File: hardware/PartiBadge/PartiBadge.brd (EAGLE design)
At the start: 101.6 x 101.6 mm, 23 parts, among them J1 I2C, J2 Supply

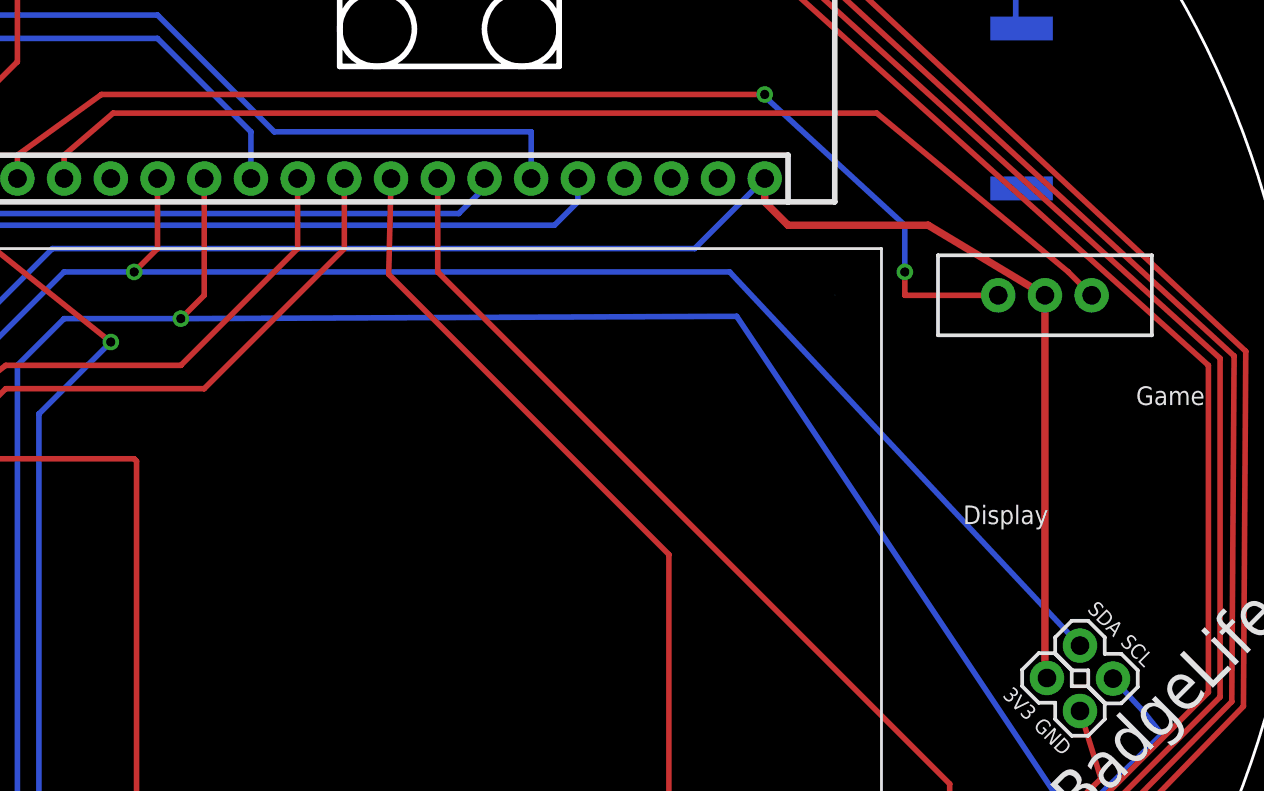
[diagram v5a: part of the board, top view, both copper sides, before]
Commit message: Add clr to 3v3 line next to switch; closes #9; add text to back; closes #8
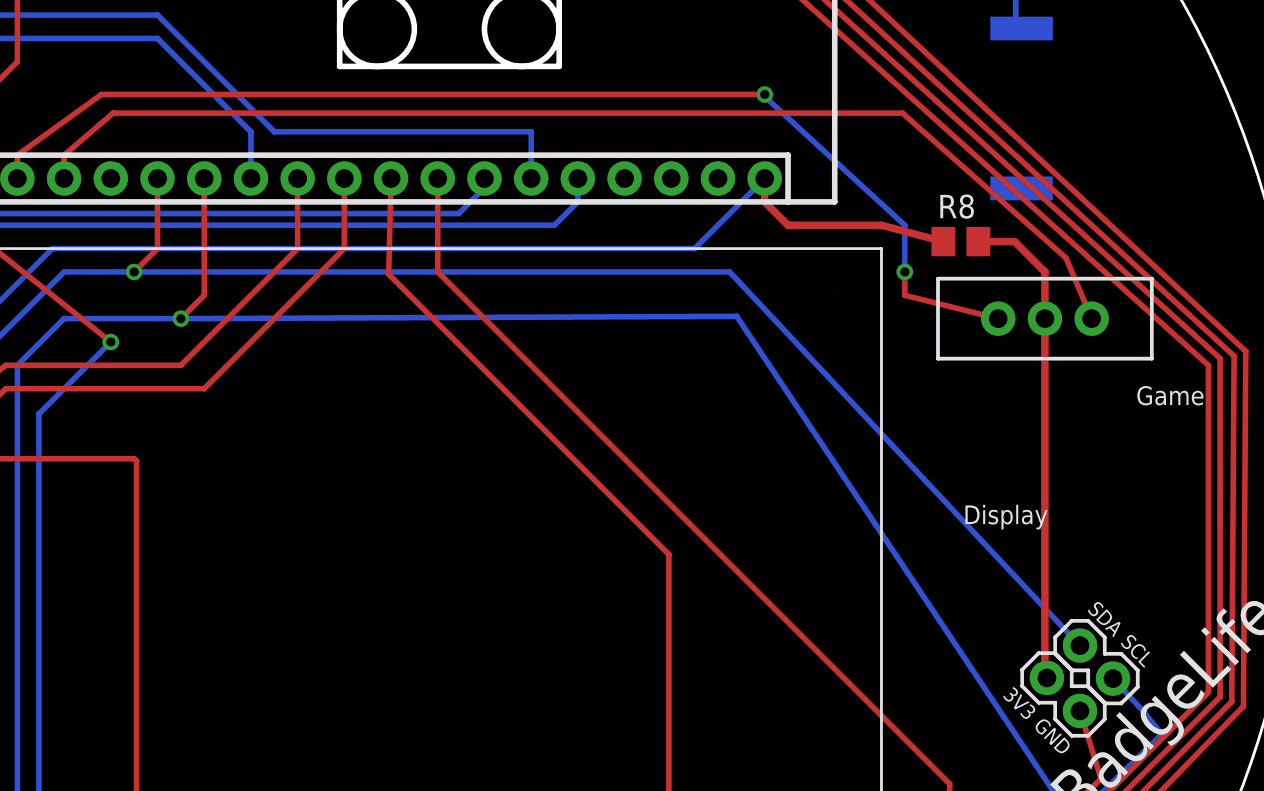
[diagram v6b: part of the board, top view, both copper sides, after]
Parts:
- added R8: 100, rcl:M0805
- moved PARTIFRAME 6.35 mm to (-1.27, 10.2)
- moved S5 1.27 mm to (90.2, 64.8)
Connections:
- net 3V3: now also R8.1, R8.2
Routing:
- net N$3: track 61.6 -> 63.2 mm
- net 3V3: track 135.5 -> 134.6 mm
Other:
- board text added: "Designed by The Particle Team http://Particle.io"
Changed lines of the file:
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@@
 <wire x1="51.816" y1="78.486" x2="63.754" y2="78.486" width="0.3048" layer="46"/>
 <wire x1="63.754" y1="78.486" x2="63.754" y2="82.55" width="0.3048" layer="46"/>
+<text x="57.15" y="50.8" size="3.81" layer="22" font="vector" ratio="18" rot="MR0" align="center">Designed by
+The Particle Team
+http://Particle.io</text>
 </plain>
 <attributes>
@@
 <attribute name="SF_SKU" value="COM-10442" x="29.21" y="24.13" size="1.778" layer="27" display="off"/>
 </element>
-<element name="S5" library="SparkFun-Switches" library_urn="urn:adsk.eagle:library:535" package="SWITCH_SPDT_PTH_11.6X4.0MM" package3d_urn="urn:adsk.eagle:package:40177/1" value="" x="90.17" y="66.04" smashed="yes" rot="R90">
-<attribute name="PROD_ID" value="SWCH-08261" x="90.17" y="66.04" size="1.778" layer="27" rot="R90" display="off"/>
-<attribute name="SF_SKU" value="COM-00102" x="90.17" y="66.04" size="1.778" layer="27" rot="R90" display="off"/>
-<attribute name="VALUE" x="90.17" y="68.453" size="0.6096" layer="27" font="vector" ratio="20" rot="R180" align="top-center"/>
+<element name="S5" library="SparkFun-Switches" library_urn="urn:adsk.eagle:library:535" package="SWITCH_SPDT_PTH_11.6X4.0MM" package3d_urn="urn:adsk.eagle:package:40177/1" value="" x="90.17" y="64.77" smashed="yes" rot="R90">
+<attribute name="PROD_ID" value="SWCH-08261" x="90.17" y="64.77" size="1.778" layer="27" rot="R90" display="off"/>
+<attribute name="SF_SKU" value="COM-00102" x="90.17" y="64.77" size="1.778" layer="27" rot="R90" display="off"/>
+<attribute name="VALUE" x="90.17" y="67.183" size="0.6096" layer="27" font="vector" ratio="20" rot="R180" align="top-center"/>
 </element>
 <element name="SJ1" library="jumper" library_urn="urn:adsk.eagle:library:252" package="SJ_2" package3d_urn="urn:adsk.eagle:package:15474/1" value="" x="15.367" y="32.131" rot="MR180"/>
@@
 <attribute name="SF_SKU" value="COM-10063" x="11.43" y="53.34" size="1.778" layer="27" rot="R315" display="off"/>
 </element>
-<element name="PARTIFRAME" library="SparkFun-Aesthetics" library_urn="urn:adsk.eagle:library:507" package="DUMMY" package3d_urn="urn:adsk.eagle:package:37104/1" value="FRAME-LETTERNO_PACKAGE" x="2.54" y="5.08">
-<attribute name="DESIGNER" value="Brandon Satrom" x="2.54" y="5.08" size="1.778" layer="27" display="off"/>
-<attribute name="VERSION" value="v01" x="2.54" y="5.08" size="1.778" layer="27" display="off"/>
+<element name="PARTIFRAME" library="SparkFun-Aesthetics" library_urn="urn:adsk.eagle:library:507" package="DUMMY" package3d_urn="urn:adsk.eagle:package:37104/1" value="FRAME-LETTERNO_PACKAGE" x="-1.27" y="10.16">
+<attribute name="DESIGNER" value="Brandon Satrom" x="-1.27" y="10.16" size="1.778" layer="27" display="off"/>
+<attribute name="VERSION" value="v01" x="-1.27" y="10.16" size="1.778" layer="27" display="off"/>
+</element>
+<element name="R8" library="rcl" library_urn="urn:adsk.eagle:library:334" package="M0805" package3d_urn="urn:adsk.eagle:package:23556/1" value="100" x="85.598" y="68.961">
+<attribute name="SPICEPREFIX" value="R" x="85.598" y="68.961" size="1.778" layer="27" display="off"/>
 </element>
 </elements>
@@
 <contactref element="S5" pad="1"/>
 <contactref element="ELECTRON" pad="20"/>
-<wire x1="87.63" y1="66.04" x2="82.55" y2="66.04" width="0.3048" layer="1"/>
+<wire x1="87.63" y1="64.77" x2="82.55" y2="66.04" width="0.3048" layer="1"/>
 <wire x1="82.55" y1="66.04" x2="82.55" y2="67.31" width="0.3048" layer="1"/>
 <via x="82.55" y="67.31" extent="1-16" drill="0.5"/>
@@
 <contactref element="S5" pad="3"/>
 <contactref element="ELECTRON" pad="21"/>
-<wire x1="92.71" y1="66.04" x2="91.44" y2="67.31" width="0.3048" layer="1"/>
-<wire x1="91.44" y1="67.31" x2="81.026" y2="75.946" width="0.3048" layer="1"/>
-<wire x1="81.026" y1="75.946" x2="39.497" y2="75.946" width="0.3048" layer="1"/>
+<wire x1="92.71" y1="64.77" x2="91.313" y2="68.072" width="0.3048" layer="1"/>
+<wire x1="91.313" y1="68.072" x2="82.423" y2="75.946" width="0.3048" layer="1"/>
+<wire x1="82.423" y1="75.946" x2="39.497" y2="75.946" width="0.3048" layer="1"/>
 <wire x1="39.497" y1="75.946" x2="36.83" y2="73.66" width="0.3048" layer="1"/>
 <wire x1="36.83" y1="73.66" x2="36.83" y2="72.39" width="0.3048" layer="1"/>
@@
 <wire x1="27.305" y1="60.325" x2="27.94" y2="60.325" width="0.3048" layer="16"/>
 <wire x1="14.644" y1="46.394" x2="27.305" y2="60.325" width="0.4064" layer="16"/>
-<wire x1="90.278946875" y1="45.23005" x2="90.17" y2="45.338996875" width="0.3048" layer="1"/>
-<wire x1="83.82" y1="69.85" x2="76.2" y2="69.85" width="0.4064" layer="1"/>
+<wire x1="90.17" y1="45.338996875" x2="90.278946875" y2="45.23005" width="0.3048" layer="1"/>
 <wire x1="76.2" y1="69.85" x2="74.93" y2="71.12" width="0.4064" layer="1"/>
 <wire x1="74.93" y1="71.12" x2="74.93" y2="72.39" width="0.4064" layer="1"/>
-<contactref element="S5" pad="2"/>
-<wire x1="90.17" y1="45.338996875" x2="90.17" y2="66.04" width="0.4064" layer="1"/>
-<wire x1="90.17" y1="66.04" x2="83.82" y2="69.85" width="0.4064" layer="1"/>
 <wire x1="27.94" y1="60.325" x2="36.195" y2="68.58" width="0.3048" layer="16"/>
 <wire x1="71.12" y1="68.58" x2="74.93" y2="72.39" width="0.3048" layer="16"/>
 <wire x1="36.195" y1="68.58" x2="71.12" y2="68.58" width="0.3048" layer="16"/>
+<wire x1="76.2" y1="69.85" x2="81.28" y2="69.85" width="0.4064" layer="1"/>
+<contactref element="R8" pad="2"/>
+<contactref element="S5" pad="2"/>
+<contactref element="R8" pad="1"/>
+<wire x1="81.28" y1="69.85" x2="84.648" y2="68.961" width="0.4064" layer="1"/>
+<wire x1="86.548" y1="68.961" x2="88.519" y2="68.961" width="0.4064" layer="1"/>
+<wire x1="88.519" y1="68.961" x2="90.17" y2="67.31" width="0.4064" layer="1"/>
+<wire x1="90.17" y1="67.31" x2="90.17" y2="64.77" width="0.4064" layer="1"/>
+<wire x1="90.17" y1="64.77" x2="90.17" y2="45.338996875" width="0.4064" layer="1"/>
+<wire x1="84.648" y1="68.961" x2="86.548" y2="68.961" width="0" layer="19" extent="1-1"/>
 </signal>
 <signal name="N$4">
@@
 </drawing>
 <compatibility>
+<note version="6.3" minversion="6.2.2" severity="warning">
+Since Version 6.2.2 text objects can contain more than one line,
+which will not be processed correctly with this version.
+</note>
 <note version="8.2" severity="warning">
 Since Version 8.2, EAGLE supports online libraries. The ids

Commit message: fix schematic and board with clr
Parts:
- moved R8 0.38 mm to (86.0, 69.0), turned to 180 degrees
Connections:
- new net N$14: R8.1, S5.2
- net 3V3: no longer R8.1, S5.2
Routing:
- net N$14: track 0.00 -> 6.46 mm
- net 3V3: track 134.6 -> 139.8 mm
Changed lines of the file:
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@@
 <attribute name="VERSION" value="v01" x="-1.27" y="10.16" size="1.778" layer="27" display="off"/>
 </element>
-<element name="R8" library="rcl" library_urn="urn:adsk.eagle:library:334" package="M0805" package3d_urn="urn:adsk.eagle:package:23556/1" value="100" x="85.598" y="68.961">
-<attribute name="SPICEPREFIX" value="R" x="85.598" y="68.961" size="1.778" layer="27" display="off"/>
+<element name="R8" library="rcl" library_urn="urn:adsk.eagle:library:334" package="M0805" package3d_urn="urn:adsk.eagle:package:23556/1" value="100" x="85.979" y="68.961" rot="R180">
+<attribute name="SPICEPREFIX" value="R" x="85.979" y="68.961" size="1.778" layer="27" rot="R180" display="off"/>
 </element>
 </elements>
@@
 <wire x1="76.2" y1="69.85" x2="81.28" y2="69.85" width="0.4064" layer="1"/>
 <contactref element="R8" pad="2"/>
-<contactref element="S5" pad="2"/>
-<contactref element="R8" pad="1"/>
-<wire x1="81.28" y1="69.85" x2="84.648" y2="68.961" width="0.4064" layer="1"/>
-<wire x1="86.548" y1="68.961" x2="88.519" y2="68.961" width="0.4064" layer="1"/>
-<wire x1="88.519" y1="68.961" x2="90.17" y2="67.31" width="0.4064" layer="1"/>
-<wire x1="90.17" y1="67.31" x2="90.17" y2="64.77" width="0.4064" layer="1"/>
-<wire x1="90.17" y1="64.77" x2="90.17" y2="45.338996875" width="0.4064" layer="1"/>
-<wire x1="84.648" y1="68.961" x2="86.548" y2="68.961" width="0" layer="19" extent="1-1"/>
+<wire x1="82.169" y1="68.961" x2="81.28" y2="69.85" width="0.4064" layer="1"/>
+<wire x1="85.029" y1="68.961" x2="82.169" y2="68.961" width="0.4064" layer="1"/>
+<wire x1="81.28" y1="69.85" x2="81.28" y2="50.8" width="0.4064" layer="1"/>
+<wire x1="81.28" y1="50.8" x2="83.82" y2="46.99" width="0.4064" layer="1"/>
+<wire x1="88.518996875" y1="46.99" x2="90.278946875" y2="45.23005" width="0.4064" layer="1"/>
+<wire x1="83.82" y1="46.99" x2="88.518996875" y2="46.99" width="0.4064" layer="1"/>
 </signal>
 <signal name="N$4">
@@
 <wire x1="10.16" y1="68.58" x2="11.43" y2="69.85" width="0.3048" layer="1"/>
 </signal>
+<signal name="N$14">
+<contactref element="S5" pad="2"/>
+<contactref element="R8" pad="1"/>
+<wire x1="90.17" y1="64.77" x2="90.17" y2="67.31" width="0.3048" layer="1"/>
+<wire x1="90.17" y1="67.31" x2="88.519" y2="68.961" width="0.3048" layer="1"/>
+<wire x1="88.519" y1="68.961" x2="86.929" y2="68.961" width="0.3048" layer="1"/>
+</signal>
 </signals>

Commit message: cleaning up routes
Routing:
- net BUTTON_YELLOW: track 57.3 -> 65.9 mm
- net SCL: track 146.7 -> 143.2 mm
- net N$6: track 136.8 -> 133.6 mm
- net LEFT: track 88.8 -> 91.2 mm
- net N$9: track 206.5 -> 204.8 mm
- net UP: track 63.8 -> 62.4 mm
- net GND: track 47.9 -> 48.9 mm
- net LED_GREEN: track 157.8 -> 157.3 mm
- net RIGHT: track 85.8 -> 86.3 mm
- net LED_BLUE: track 179.3 -> 178.8 mm
